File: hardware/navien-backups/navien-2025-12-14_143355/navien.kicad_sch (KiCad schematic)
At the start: 26 parts, among them J1 Conn_01x03_MountingPin, J2 Conn_01x02, J3 S6B-XH-SM4-TB, Q1 2n7002, U1 WeMos_D1_mini, U2 THVD1406DR, U3 LM7805_TO220

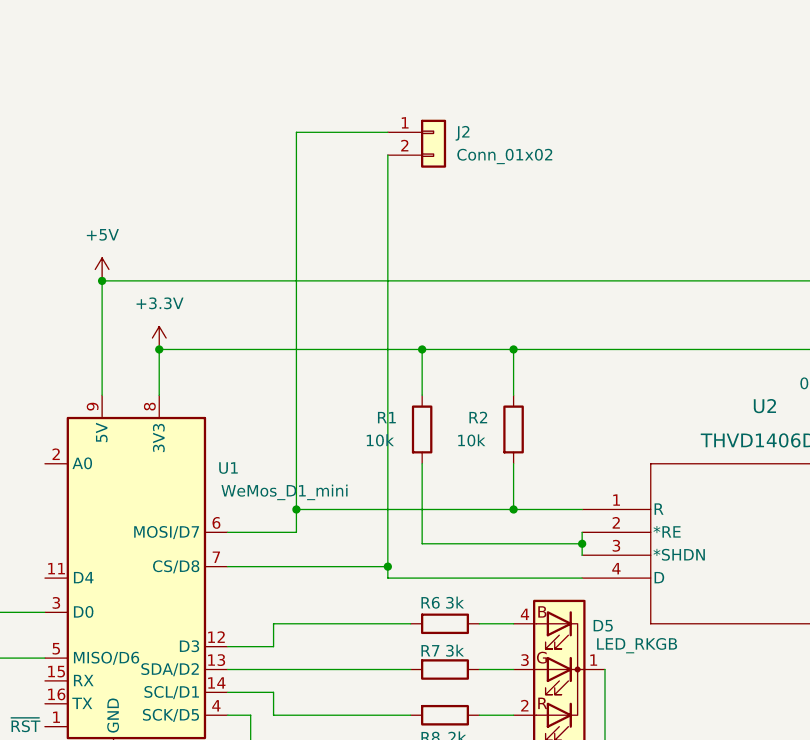
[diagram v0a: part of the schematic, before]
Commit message: doc: consolidate Navien 240 documentation (240A/240A2): add doc/240.md, update README, remove doc/240-a.md
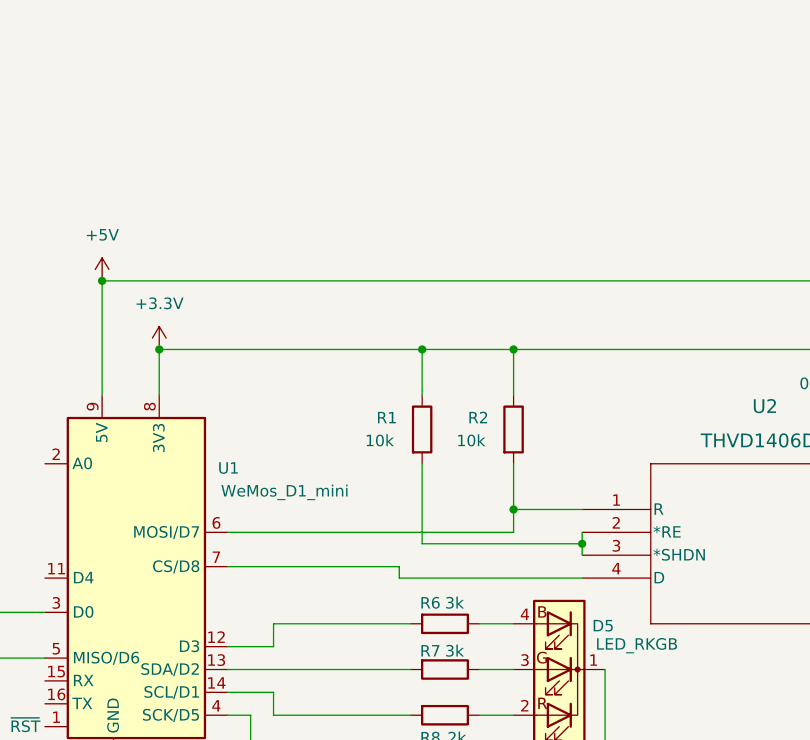
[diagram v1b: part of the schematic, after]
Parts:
- removed J2: Conn_01x02, Connector_PinHeader_2.54mm:PinHeader_1x02_P2.54mm_Vertical, symbol Connector_Generic:Conn_01x02
- D1, D5: footprint BIVAR_PIPE:LED-ARRAY-SMD_4P-L1.6-W1.5-BL-FD-WITH-PIPE-2 -> LED-ARRAY-SMD_4P-L1.6-W1.5-BL-FD
- J3: footprint S6B_XH_SM4_TB:CONN_S6B-XH-SM4-TB_JST -> CONN_S6B-XH-SM4-TB_JST
- U2: footprint THVD1406DR:SOIC_D0008A_TEX -> SOIC_D0008A_TEX
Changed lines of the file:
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@@
-	)
-	(junction
-		(at 102.87 95.25)
-		(diameter 0)
-		(color 0 0 0 0)
-	)
-	(junction
-		(at 92.71 88.9)
-		(diameter 0)
-		(color 0 0 0 0)
 	)
 	(junction
@@
 	(wire
 		(pts
-			(xy 92.71 91.44) (xy 92.71 88.9)
-		)
-		(stroke
-			(width 0)
-			(type default)
-		)
-	)
-	(wire
-		(pts
 			(xy 213.36 93.98) (xy 223.52 93.98)
 		)
@@
 	(wire
 		(pts
-			(xy 102.87 46.99) (xy 92.71 46.99)
-		)
-		(stroke
-			(width 0)
-			(type default)
-		)
-	)
-	(wire
-		(pts
 			(xy 127 116.84) (xy 165.1 116.84)
 		)
@@
 	(wire
 		(pts
-			(xy 92.71 46.99) (xy 92.71 88.9)
-		)
-		(stroke
-			(width 0)
-			(type default)
-		)
-	)
-	(wire
-		(pts
 			(xy 124.46 91.44) (xy 124.46 92.71)
 		)
@@
 	(wire
 		(pts
-			(xy 85.09 91.44) (xy 92.71 91.44)
-		)
-		(stroke
-			(width 0)
-			(type default)
-		)
-	)
-	(wire
-		(pts
 			(xy 165.1 88.9) (xy 165.1 78.74)
 		)
@@
 	(wire
 		(pts
+			(xy 85.09 91.44) (xy 116.84 91.44)
+		)
+		(stroke
+			(width 0)
+			(type default)
+		)
+	)
+	(wire
+		(pts
 			(xy 190.5 96.52) (xy 190.5 101.6)
 		)
@@
 	(wire
 		(pts
-			(xy 102.87 49.53) (xy 102.87 95.25)
-		)
-		(stroke
-			(width 0)
-			(type default)
-		)
-	)
-	(wire
-		(pts
 			(xy 87.63 111.76) (xy 87.63 138.43)
 		)
@@
 	(wire
 		(pts
-			(xy 102.87 96.52) (xy 124.46 96.52)
+			(xy 104.14 96.52) (xy 124.46 96.52)
 		)
 		(stroke
@@
 	(wire
 		(pts
-			(xy 85.09 95.25) (xy 102.87 95.25)
+			(xy 85.09 95.25) (xy 104.14 95.25)
 		)
 		(stroke
@@
 	(wire
 		(pts
+			(xy 116.84 91.44) (xy 116.84 88.9)
+		)
+		(stroke
+			(width 0)
+			(type default)
+		)
+	)
+	(wire
+		(pts
 			(xy 190.5 83.82) (xy 190.5 88.9)
 		)
@@
 	(wire
 		(pts
-			(xy 102.87 95.25) (xy 102.87 96.52)
+			(xy 104.14 95.25) (xy 104.14 96.52)
 		)
 		(stroke
@@
 		(pts
 			(xy 223.52 86.36) (xy 218.44 86.36)
-		)
-		(stroke
-			(width 0)
-			(type default)
-		)
-	)
-	(wire
-		(pts
-			(xy 92.71 88.9) (xy 116.84 88.9)
 		)
 		(stroke
@@
 			)
 		)
-		(property "Footprint" "S6B_XH_SM4_TB:CONN_S6B-XH-SM4-TB_JST"
+		(property "Footprint" "CONN_S6B-XH-SM4-TB_JST"
 			(at 223.52 83.82 0)
 			(effects
@@
 			)
 		)
-		(property "Footprint" "BIVAR_PIPE:LED-ARRAY-SMD_4P-L1.6-W1.5-BL-FD-WITH-PIPE-2"
+		(property "Footprint" "LED-ARRAY-SMD_4P-L1.6-W1.5-BL-FD"
 			(at 120.904 94.996 0)
 			(effects
@@
 			)
 		)
-		(property "Footprint" "THVD1406DR:SOIC_D0008A_TEX"
+		(property "Footprint" "SOIC_D0008A_TEX"
 			(at 124.46 88.9 0)
 			(effects
@@
 	)
 	(symbol
-		(lib_id "Connector_Generic:Conn_01x02")
-		(at 107.95 46.99 0)
-		(unit 1)
-		(exclude_from_sim no)
-		(in_bom yes)
-		(on_board yes)
-		(dnp no)
-		(fields_autoplaced yes)
-		(property "Reference" "J2"
-			(at 110.49 46.9899 0)
-			(effects
-				(font
-					(size 1.27 1.27)
-				)
-				(justify left)
-			)
-		)
-		(property "Value" "Conn_01x02"
-			(at 110.49 49.5299 0)
-			(effects
-				(font
-					(size 1.27 1.27)
-				)
-				(justify left)
-			)
-		)
-		(property "Footprint" "Connector_PinHeader_2.54mm:PinHeader_1x02_P2.54mm_Vertical"
-			(at 107.95 46.99 0)
-			(effects
-				(font
-					(size 1.27 1.27)
-				)
-				(hide yes)
-			)
-		)
-		(property "Datasheet" "~"
-			(at 107.95 46.99 0)
-			(effects
-				(font
-					(size 1.27 1.27)
-				)
-				(hide yes)
-			)
-		)
-		(property "Description" "Generic connector, single row, 01x02, script generated (kicad-library-utils/schlib/autogen/connector/)"
-			(at 107.95 46.99 0)
-			(effects
-				(font
-					(size 1.27 1.27)
-				)
-				(hide yes)
-			)
-		)
-		(pin "2"
-		)
-		(pin "1"
-		)
-		(instances
-			(project ""
-				(path "/0b33f629-68c1-4188-ad1f-b8b2ec65913a"
-					(reference "J2")
-					(unit 1)
-				)
-			)
-		)
-	)
-	(symbol
 		(lib_id "Device:C_Polarized")
 		(at 184.15 68.58 0)
@@
 			)
 		)
-		(property "Footprint" "BIVAR_PIPE:LED-ARRAY-SMD_4P-L1.6-W1.5-BL-FD-WITH-PIPE-2"
+		(property "Footprint" "LED-ARRAY-SMD_4P-L1.6-W1.5-BL-FD"
 			(at 45.72 110.744 0)
 			(effects
